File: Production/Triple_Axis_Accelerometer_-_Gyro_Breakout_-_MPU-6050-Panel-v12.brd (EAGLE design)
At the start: 116.8 x 107.7 mm, 459 parts, among them U1 MPU-6050-1, U10 MPU-6050-1, U11 MPU-6050-1, U12 MPU-6050-1, U13 MPU-6050-1, U14 MPU-6050-1, U15 MPU-6050-1, U16 MPU-6050-1, U17 MPU-6050-1, U18 MPU-6050-1, U19 MPU-6050-1, U2 MPU-6050-1, U20 MPU-6050-1, U21 MPU-6050-1, U22 MPU-6050-1, U23 MPU-6050-1, U24 MPU-6050-1, U3 MPU-6050-1, U4 MPU-6050-1, U5 MPU-6050-1, U6 MPU-6050-1, U7 MPU-6050-1, U8 MPU-6050-1, U9 MPU-6050-1

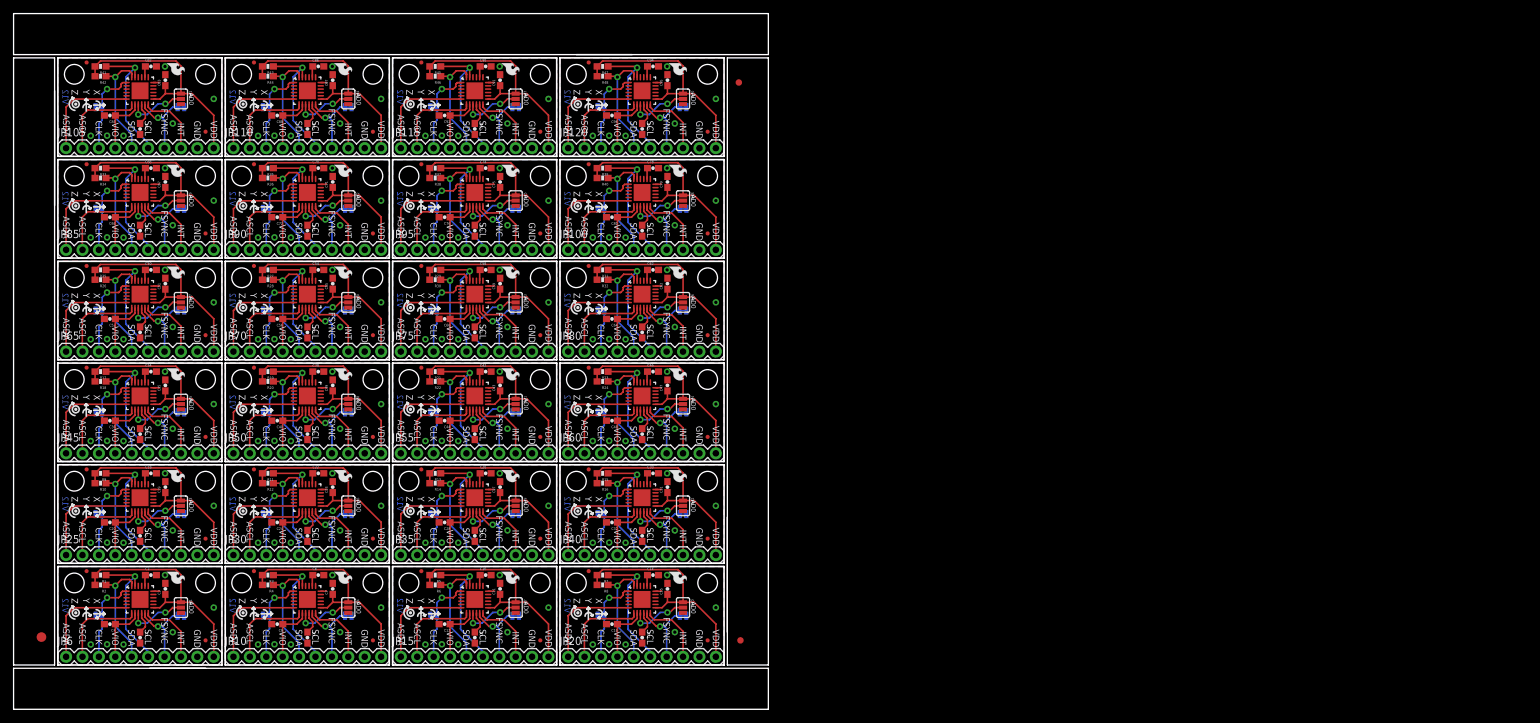
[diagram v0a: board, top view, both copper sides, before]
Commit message: changed panel for better solder printing
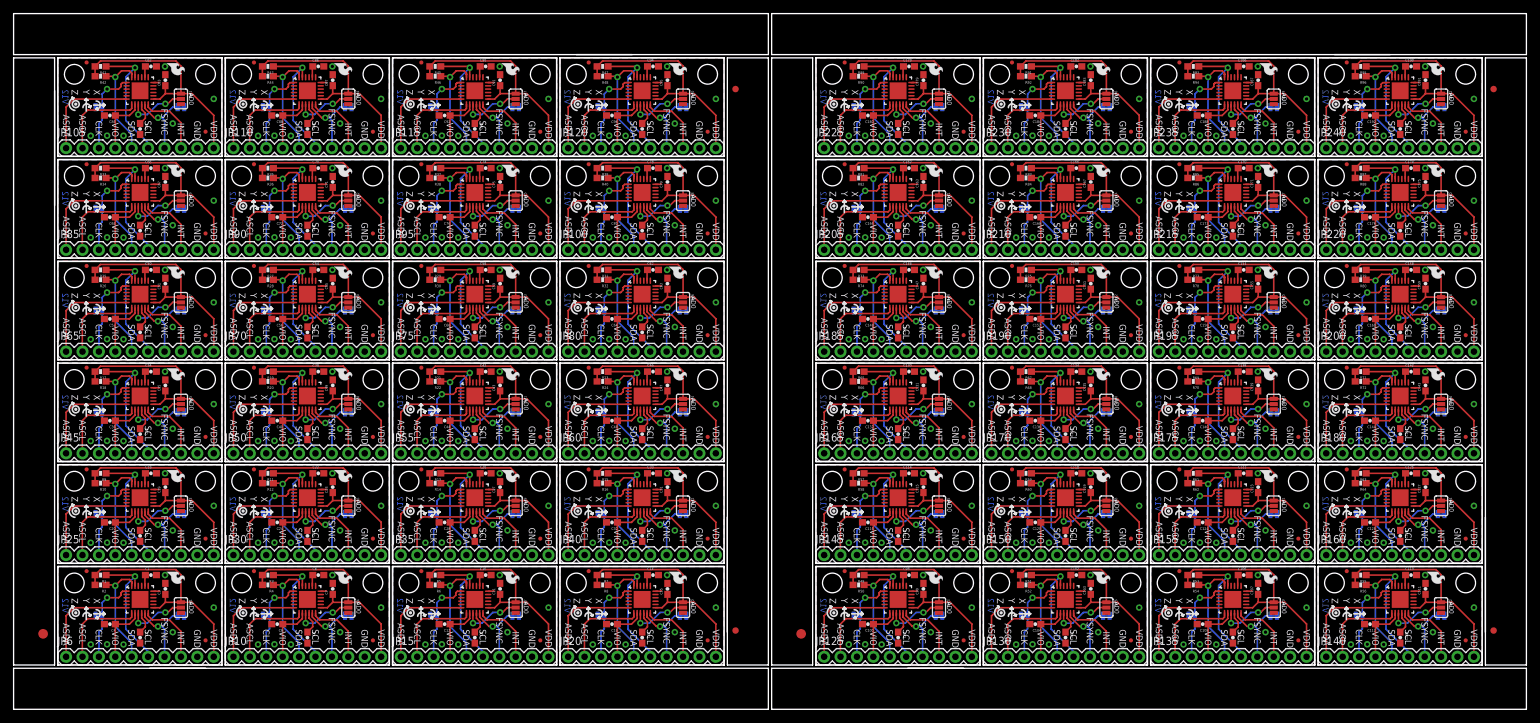
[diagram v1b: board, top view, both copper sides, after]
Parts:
- added C100, C104, C108, C112, C116, C120, C124, C128, C132, C136, C140, C144, C148, C152, C156, C160, C164, C168, C172, C176, C180, C184, C188, C192: 10nF, SparkFun:0603-CAP
- added C101, C103, C105, C107, C109, C111, C113, C115, C117, C119, C121, C123, C125, C127, C129, C131, C133, C135, C137, C139, C141, C143, C145, C147, C149, C151, C153, C155, C157, C159, C161, C163, C165, C167, C169, C171, C173, C175, C177, C179, C181, C183, C185, C187, C189, C191, C97, C99: 0.1uF, SparkFun:0603-CAP
- added C102, C106, C110, C114, C118, C122, C126, C130, C134, C138, C142, C146, C150, C154, C158, C162, C166, C170, C174, C178, C182, C186, C190, C98: 2.2nF, SparkFun:0603-CAP
- added E$2, E$3: (no value), SparkFun-Aesthetics:FIDUCIAL-1X2
- added E$6: (no value), SparkFun-Aesthetics:FIDUCIAL-1.5X3
- added JP121, JP122, JP126, JP127, JP131, JP132, JP136, JP137, JP141, JP142, JP146, JP147, JP151, JP152, JP156, JP157, JP161, JP162, JP166, JP167, JP171, JP172, JP176, JP177, JP181, JP182, JP186, JP187, JP191, JP192, JP196, JP197, JP201, JP202, JP206, JP207, JP211, JP212, JP216, JP217, JP221, JP222, JP226, JP227, JP231, JP232, JP236, JP237: STAND-OFFTIGHT, SparkFun:STAND-OFF-TIGHT
- added JP123, JP124, JP128, JP129, JP133, JP134, JP138, JP139, JP143, JP144, JP148, JP149, JP153, JP154, JP158, JP159, JP163, JP164, JP168, JP169, JP173, JP174, JP178, JP179, JP183, JP184, JP188, JP189, JP193, JP194, JP198, JP199, JP203, JP204, JP208, JP209, JP213, JP214, JP218, JP219, JP223, JP224, JP228, JP229, JP233, JP234, JP238, JP239: FIDUCIALUFIDUCIAL, SparkFun:MICRO-FIDUCIAL
- added JP125, JP130, JP135, JP140, JP145, JP150, JP155, JP160, JP165, JP170, JP175, JP180, JP185, JP190, JP195, JP200, JP205, JP210, JP215, JP220, JP225, JP230, JP235, JP240: M10", SparkFun:1X10
- added R49, R50, R51, R52, R53, R54, R55, R56, R57, R58, R59, R60, R61, R62, R63, R64, R65, R66, R67, R68, R69, R70, R71, R72, R73, R74, R75, R76, R77, R78, R79, R80, R81, R82, R83, R84, R85, R86, R87, R88, R89, R90, R91, R92, R93, R94, R95, R96: 10k, SparkFun:0603-RES
- added SJ100, SJ103, SJ106, SJ109, SJ112, SJ115, SJ118, SJ121, SJ124, SJ127, SJ130, SJ133, SJ136, SJ139, SJ142, SJ73, SJ76, SJ79, SJ82, SJ85, SJ88, SJ91, SJ94, SJ97: (no value), SparkFun:SJ_3_PASTE2&3
- added SJ101, SJ102, SJ104, SJ105, SJ107, SJ108, SJ110, SJ111, SJ113, SJ114, SJ116, SJ117, SJ119, SJ120, SJ122, SJ123, SJ125, SJ126, SJ128, SJ129, SJ131, SJ132, SJ134, SJ135, SJ137, SJ138, SJ140, SJ141, SJ143, SJ144, SJ74, SJ75, SJ77, SJ78, SJ80, SJ81, SJ83, SJ84, SJ86, SJ87, SJ89, SJ90, SJ92, SJ93, SJ95, SJ96, SJ98, SJ99: (no value), SparkFun:SJ_2S-TRACE
- added U$100, U$104, U$108, U$112, U$116, U$120, U$124, U$128, U$132, U$136, U$140, U$144, U$148, U$152, U$156, U$160, U$164, U$168, U$172, U$176, U$180, U$184, U$188, U$192: (no value), SparkFun:SFE-NEW-WEB
- added U$101, U$103, U$105, U$107, U$109, U$111, U$113, U$115, U$117, U$119, U$121, U$123, U$125, U$127, U$129, U$131, U$133, U$135, U$137, U$139, U$141, U$143, U$145, U$147, U$149, U$151, U$153, U$155, U$157, U$159, U$161, U$163, U$165, U$167, U$169, U$171, U$173, U$175, U$177, U$179, U$181, U$183, U$185, U$187, U$189, U$191, U$97, U$99: (no value), SparkFun:SFE-LOGO-FLAME
- added U$102, U$106, U$110, U$114, U$118, U$122, U$126, U$130, U$134, U$138, U$142, U$146, U$150, U$154, U$158, U$162, U$166, U$170, U$174, U$178, U$182, U$186, U$190, U$98: OSHW-LOGOS, SparkFun:OSHW-LOGO-S
- added U25, U26, U27, U28, U29, U30, U31, U32, U33, U34, U35, U36, U37, U38, U39, U40, U41, U42, U43, U44, U45, U46, U47, U48: MPU-6050-1, Testing:QFN-24-4MM2
- moved E$4 1.70 mm to (111.8, 12.2)
- moved E$5 1.14 mm to (111.8, 96.0)
- moved E$1 0.57 mm to (4.57, 11.7)
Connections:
- new net ADO24: SJ73.2, U25.9
- new net ADO25: SJ76.2, U26.9
- new net ADO26: SJ79.2, U27.9
- new net ADO27: SJ82.2, U28.9
- new net ADO28: SJ85.2, U29.9
- new net ADO29: SJ88.2, U30.9
- new net ADO30: SJ91.2, U31.9
- new net ADO31: SJ94.2, U32.9
- new net ADO32: SJ97.2, U33.9
- new net ADO33: SJ100.2, U34.9
- new net ADO34: SJ103.2, U35.9
- new net ADO35: SJ106.2, U36.9
- new net ADO36: SJ109.2, U37.9
- new net ADO37: SJ112.2, U38.9
- new net ADO38: SJ115.2, U39.9
- new net ADO39: SJ118.2, U40.9
- new net ADO40: SJ121.2, U41.9
- new net ADO41: SJ124.2, U42.9
- new net ADO42: SJ127.2, U43.9
- new net ADO43: SJ130.2, U44.9
- new net ADO44: SJ133.2, U45.9
- new net ADO45: SJ136.2, U46.9
- new net ADO46: SJ139.2, U47.9
- new net ADO47: SJ142.2, U48.9
- new net AUX_SCL24: JP125.2, U25.7
- new net AUX_SCL25: JP130.2, U26.7
- new net AUX_SCL26: JP135.2, U27.7
- new net AUX_SCL27: JP140.2, U28.7
- new net AUX_SCL28: JP145.2, U29.7
- new net AUX_SCL29: JP150.2, U30.7
- new net AUX_SCL30: JP155.2, U31.7
- new net AUX_SCL31: JP160.2, U32.7
- new net AUX_SCL32: JP165.2, U33.7
- new net AUX_SCL33: JP170.2, U34.7
- new net AUX_SCL34: JP175.2, U35.7
- new net AUX_SCL35: JP180.2, U36.7
- new net AUX_SCL36: JP185.2, U37.7
- new net AUX_SCL37: JP190.2, U38.7
- new net AUX_SCL38: JP195.2, U39.7
- new net AUX_SCL39: JP200.2, U40.7
- new net AUX_SCL40: JP205.2, U41.7
- new net AUX_SCL41: JP210.2, U42.7
- new net AUX_SCL42: JP215.2, U43.7
- new net AUX_SCL43: JP220.2, U44.7
- new net AUX_SCL44: JP225.2, U45.7
- new net AUX_SCL45: JP230.2, U46.7
- new net AUX_SCL46: JP235.2, U47.7
- new net AUX_SCL47: JP240.2, U48.7
- new net AUX_SDA24: JP125.1, U25.6
- new net AUX_SDA25: JP130.1, U26.6
- new net AUX_SDA26: JP135.1, U27.6
- new net AUX_SDA27: JP140.1, U28.6
- new net AUX_SDA28: JP145.1, U29.6
- new net AUX_SDA29: JP150.1, U30.6
- new net AUX_SDA30: JP155.1, U31.6
- new net AUX_SDA31: JP160.1, U32.6
- new net AUX_SDA32: JP165.1, U33.6
- new net AUX_SDA33: JP170.1, U34.6
- new net AUX_SDA34: JP175.1, U35.6
- new net AUX_SDA35: JP180.1, U36.6
- new net AUX_SDA36: JP185.1, U37.6
- new net AUX_SDA37: JP190.1, U38.6
- new net AUX_SDA38: JP195.1, U39.6
- new net AUX_SDA39: JP200.1, U40.6
- new net AUX_SDA40: JP205.1, U41.6
- new net AUX_SDA41: JP210.1, U42.6
- new net AUX_SDA42: JP215.1, U43.6
- new net AUX_SDA43: JP220.1, U44.6
- new net AUX_SDA44: JP225.1, U45.6
- new net AUX_SDA45: JP230.1, U46.6
- new net AUX_SDA46: JP235.1, U47.6
- new net AUX_SDA47: JP240.1, U48.6
- new net CLKIN24: JP125.3, SJ75.2, U25.1
- new net CLKIN25: JP130.3, SJ78.2, U26.1
- new net CLKIN26: JP135.3, SJ81.2, U27.1
- new net CLKIN27: JP140.3, SJ84.2, U28.1
- new net CLKIN28: JP145.3, SJ87.2, U29.1
- new net CLKIN29: JP150.3, SJ90.2, U30.1
- new net CLKIN30: JP155.3, SJ93.2, U31.1
- new net CLKIN31: JP160.3, SJ96.2, U32.1
- new net CLKIN32: JP165.3, SJ99.2, U33.1
- new net CLKIN33: JP170.3, SJ102.2, U34.1
- new net CLKIN34: JP175.3, SJ105.2, U35.1
- new net CLKIN35: JP180.3, SJ108.2, U36.1
- new net CLKIN36: JP185.3, SJ111.2, U37.1
- new net CLKIN37: JP190.3, SJ114.2, U38.1
- new net CLKIN38: JP195.3, SJ117.2, U39.1
- new net CLKIN39: JP200.3, SJ120.2, U40.1
- new net CLKIN40: JP205.3, SJ123.2, U41.1
- new net CLKIN41: JP210.3, SJ126.2, U42.1
- new net CLKIN42: JP215.3, SJ129.2, U43.1
- new net CLKIN43: JP220.3, SJ132.2, U44.1
- new net CLKIN44: JP225.3, SJ135.2, U45.1
- new net CLKIN45: JP230.3, SJ138.2, U46.1
- new net CLKIN46: JP235.3, SJ141.2, U47.1
- new net CLKIN47: JP240.3, SJ144.2, U48.1
- new net FSYNC24: JP125.7, SJ74.2, U25.11
- new net FSYNC25: JP130.7, SJ77.2, U26.11
- new net FSYNC26: JP135.7, SJ80.2, U27.11
- new net FSYNC27: JP140.7, SJ83.2, U28.11
- new net FSYNC28: JP145.7, SJ86.2, U29.11
- new net FSYNC29: JP150.7, SJ89.2, U30.11
- new net FSYNC30: JP155.7, SJ92.2, U31.11
- new net FSYNC31: JP160.7, SJ95.2, U32.11
- new net FSYNC32: JP165.7, SJ98.2, U33.11
- new net FSYNC33: JP170.7, SJ101.2, U34.11
- new net FSYNC34: JP175.7, SJ104.2, U35.11
- new net FSYNC35: JP180.7, SJ107.2, U36.11
- new net FSYNC36: JP185.7, SJ110.2, U37.11
- new net FSYNC37: JP190.7, SJ113.2, U38.11
- new net FSYNC38: JP195.7, SJ116.2, U39.11
- new net FSYNC39: JP200.7, SJ119.2, U40.11
- new net FSYNC40: JP205.7, SJ122.2, U41.11
- new net FSYNC41: JP210.7, SJ125.2, U42.11
- new net FSYNC42: JP215.7, SJ128.2, U43.11
- new net FSYNC43: JP220.7, SJ131.2, U44.11
- new net FSYNC44: JP225.7, SJ134.2, U45.11
- new net FSYNC45: JP230.7, SJ137.2, U46.11
- new net FSYNC46: JP235.7, SJ140.2, U47.11
- new net FSYNC47: JP240.7, SJ143.2, U48.11
- new net GND24: C100.2, C97.2, C98.2, C99.2, JP125.9, SJ73.3, SJ74.1, SJ75.1, U25.18
- new net GND25: C101.2, C102.2, C103.2, C104.2, JP130.9, SJ76.3, SJ77.1, SJ78.1, U26.18
- new net GND26: C105.2, C106.2, C107.2, C108.2, JP135.9, SJ79.3, SJ80.1, SJ81.1, U27.18
- new net GND27: C109.2, C110.2, C111.2, C112.2, JP140.9, SJ82.3, SJ83.1, SJ84.1, U28.18
- new net GND28: C113.2, C114.2, C115.2, C116.2, JP145.9, SJ85.3, SJ86.1, SJ87.1, U29.18
- new net GND29: C117.2, C118.2, C119.2, C120.2, JP150.9, SJ88.3, SJ89.1, SJ90.1, U30.18
- new net GND30: C121.2, C122.2, C123.2, C124.2, JP155.9, SJ91.3, SJ92.1, SJ93.1, U31.18
- new net GND31: C125.2, C126.2, C127.2, C128.2, JP160.9, SJ94.3, SJ95.1, SJ96.1, U32.18
- new net GND32: C129.2, C130.2, C131.2, C132.2, JP165.9, SJ97.3, SJ98.1, SJ99.1, U33.18
- new net GND33: C133.2, C134.2, C135.2, C136.2, JP170.9, SJ100.3, SJ101.1, SJ102.1, U34.18
- new net GND34: C137.2, C138.2, C139.2, C140.2, JP175.9, SJ103.3, SJ104.1, SJ105.1, U35.18
- new net GND35: C141.2, C142.2, C143.2, C144.2, JP180.9, SJ106.3, SJ107.1, SJ108.1, U36.18
- new net GND36: C145.2, C146.2, C147.2, C148.2, JP185.9, SJ109.3, SJ110.1, SJ111.1, U37.18
- new net GND37: C149.2, C150.2, C151.2, C152.2, JP190.9, SJ112.3, SJ113.1, SJ114.1, U38.18
- new net GND38: C153.2, C154.2, C155.2, C156.2, JP195.9, SJ115.3, SJ116.1, SJ117.1, U39.18
- new net GND39: C157.2, C158.2, C159.2, C160.2, JP200.9, SJ118.3, SJ119.1, SJ120.1, U40.18
- new net GND40: C161.2, C162.2, C163.2, C164.2, JP205.9, SJ121.3, SJ122.1, SJ123.1, U41.18
- new net GND41: C165.2, C166.2, C167.2, C168.2, JP210.9, SJ124.3, SJ125.1, SJ126.1, U42.18
- new net GND42: C169.2, C170.2, C171.2, C172.2, JP215.9, SJ127.3, SJ128.1, SJ129.1, U43.18
- new net GND43: C173.2, C174.2, C175.2, C176.2, JP220.9, SJ130.3, SJ131.1, SJ132.1, U44.18
- new net GND44: C177.2, C178.2, C179.2, C180.2, JP225.9, SJ133.3, SJ134.1, SJ135.1, U45.18
- new net GND45: C181.2, C182.2, C183.2, C184.2, JP230.9, SJ136.3, SJ137.1, SJ138.1, U46.18
- new net GND46: C185.2, C186.2, C187.2, C188.2, JP235.9, SJ139.3, SJ140.1, SJ141.1, U47.18
- new net GND47: C189.2, C190.2, C191.2, C192.2, JP240.9, SJ142.3, SJ143.1, SJ144.1, U48.18
- new net INT24: JP125.8, U25.12
- new net INT25: JP130.8, U26.12
- new net INT26: JP135.8, U27.12
- new net INT27: JP140.8, U28.12
- new net INT28: JP145.8, U29.12
- new net INT29: JP150.8, U30.12
- new net INT30: JP155.8, U31.12
- new net INT31: JP160.8, U32.12
- new net INT32: JP165.8, U33.12
- new net INT33: JP170.8, U34.12
- new net INT34: JP175.8, U35.12
- new net INT35: JP180.8, U36.12
- new net INT36: JP185.8, U37.12
- new net INT37: JP190.8, U38.12
- new net INT38: JP195.8, U39.12
- new net INT39: JP200.8, U40.12
- new net INT40: JP205.8, U41.12
- new net INT41: JP210.8, U42.12
- new net INT42: JP215.8, U43.12
- new net INT43: JP220.8, U44.12
- new net INT44: JP225.8, U45.12
- new net INT45: JP230.8, U46.12
- new net INT46: JP235.8, U47.12
- new net INT47: JP240.8, U48.12
- new net N$49: C98.1, U25.20
- new net N$50: C97.1, U25.10
- new net N$51: C102.1, U26.20
- new net N$52: C101.1, U26.10
- new net N$53: C106.1, U27.20
- new net N$54: C105.1, U27.10
- new net N$55: C110.1, U28.20
- new net N$56: C109.1, U28.10
- new net N$57: C114.1, U29.20
- new net N$58: C113.1, U29.10
- new net N$59: C118.1, U30.20
- new net N$60: C117.1, U30.10
- new net N$61: C122.1, U31.20
- new net N$62: C121.1, U31.10
- new net N$63: C126.1, U32.20
- new net N$64: C125.1, U32.10
- new net N$65: C130.1, U33.20
- new net N$66: C129.1, U33.10
- new net N$67: C134.1, U34.20
- new net N$68: C133.1, U34.10
- new net N$69: C138.1, U35.20
- new net N$70: C137.1, U35.10
- new net N$71: C142.1, U36.20
- new net N$72: C141.1, U36.10
- new net N$73: C146.1, U37.20
- new net N$74: C145.1, U37.10
- new net N$75: C150.1, U38.20
- new net N$76: C149.1, U38.10
- new net N$77: C154.1, U39.20
- new net N$78: C153.1, U39.10
- new net N$79: C158.1, U40.20
- new net N$80: C157.1, U40.10
- new net N$81: C162.1, U41.20
- new net N$82: C161.1, U41.10
- new net N$83: C166.1, U42.20
- new net N$84: C165.1, U42.10
- new net N$85: C170.1, U43.20
- new net N$86: C169.1, U43.10
- new net N$87: C174.1, U44.20
- new net N$88: C173.1, U44.10
- new net N$89: C178.1, U45.20
- new net N$90: C177.1, U45.10
- new net N$91: C182.1, U46.20
- new net N$92: C181.1, U46.10
- new net N$93: C186.1, U47.20
- new net N$94: C185.1, U47.10
- new net N$95: C190.1, U48.20
- new net N$96: C189.1, U48.10
- new net SCL24: JP125.6, R49.1, U25.23
- new net SCL25: JP130.6, R51.1, U26.23
- new net SCL26: JP135.6, R53.1, U27.23
- new net SCL27: JP140.6, R55.1, U28.23
- new net SCL28: JP145.6, R57.1, U29.23
- new net SCL29: JP150.6, R59.1, U30.23
- new net SCL30: JP155.6, R61.1, U31.23
- new net SCL31: JP160.6, R63.1, U32.23
- new net SCL32: JP165.6, R65.1, U33.23
- new net SCL33: JP170.6, R67.1, U34.23
- new net SCL34: JP175.6, R69.1, U35.23
- new net SCL35: JP180.6, R71.1, U36.23
- new net SCL36: JP185.6, R73.1, U37.23
- new net SCL37: JP190.6, R75.1, U38.23
- new net SCL38: JP195.6, R77.1, U39.23
- new net SCL39: JP200.6, R79.1, U40.23
- new net SCL40: JP205.6, R81.1, U41.23
- new net SCL41: JP210.6, R83.1, U42.23
- new net SCL42: JP215.6, R85.1, U43.23
- new net SCL43: JP220.6, R87.1, U44.23
- new net SCL44: JP225.6, R89.1, U45.23
- new net SCL45: JP230.6, R91.1, U46.23
- new net SCL46: JP235.6, R93.1, U47.23
- new net SCL47: JP240.6, R95.1, U48.23
- new net SDA24: JP125.5, R50.1, U25.24
- new net SDA25: JP130.5, R52.1, U26.24
- new net SDA26: JP135.5, R54.1, U27.24
- new net SDA27: JP140.5, R56.1, U28.24
- new net SDA28: JP145.5, R58.1, U29.24
- new net SDA29: JP150.5, R60.1, U30.24
- new net SDA30: JP155.5, R62.1, U31.24
- new net SDA31: JP160.5, R64.1, U32.24
- new net SDA32: JP165.5, R66.1, U33.24
- new net SDA33: JP170.5, R68.1, U34.24
- new net SDA34: JP175.5, R70.1, U35.24
- new net SDA35: JP180.5, R72.1, U36.24
- new net SDA36: JP185.5, R74.1, U37.24
- new net SDA37: JP190.5, R76.1, U38.24
- new net SDA38: JP195.5, R78.1, U39.24
- new net SDA39: JP200.5, R80.1, U40.24
- new net SDA40: JP205.5, R82.1, U41.24
- new net SDA41: JP210.5, R84.1, U42.24
- new net SDA42: JP215.5, R86.1, U43.24
- new net SDA43: JP220.5, R88.1, U44.24
- new net SDA44: JP225.5, R90.1, U45.24
- new net SDA45: JP230.5, R92.1, U46.24
- new net SDA46: JP235.5, R94.1, U47.24
- new net SDA47: JP240.5, R96.1, U48.24
- new net VCC24: C99.1, JP125.10, R49.2, R50.2, SJ73.1, U25.13
- new net VCC25: C103.1, JP130.10, R51.2, R52.2, SJ76.1, U26.13
- new net VCC26: C107.1, JP135.10, R53.2, R54.2, SJ79.1, U27.13
- new net VCC27: C111.1, JP140.10, R55.2, R56.2, SJ82.1, U28.13
- new net VCC28: C115.1, JP145.10, R57.2, R58.2, SJ85.1, U29.13
- new net VCC29: C119.1, JP150.10, R59.2, R60.2, SJ88.1, U30.13
- new net VCC30: C123.1, JP155.10, R61.2, R62.2, SJ91.1, U31.13
- new net VCC31: C127.1, JP160.10, R63.2, R64.2, SJ94.1, U32.13
- new net VCC32: C131.1, JP165.10, R65.2, R66.2, SJ97.1, U33.13
- new net VCC33: C135.1, JP170.10, R67.2, R68.2, SJ100.1, U34.13
- new net VCC34: C139.1, JP175.10, R69.2, R70.2, SJ103.1, U35.13
- new net VCC35: C143.1, JP180.10, R71.2, R72.2, SJ106.1, U36.13
- new net VCC36: C147.1, JP185.10, R73.2, R74.2, SJ109.1, U37.13
- new net VCC37: C151.1, JP190.10, R75.2, R76.2, SJ112.1, U38.13
- new net VCC38: C155.1, JP195.10, R77.2, R78.2, SJ115.1, U39.13
- new net VCC39: C159.1, JP200.10, R79.2, R80.2, SJ118.1, U40.13
- new net VCC40: C163.1, JP205.10, R81.2, R82.2, SJ121.1, U41.13
- new net VCC41: C167.1, JP210.10, R83.2, R84.2, SJ124.1, U42.13
- new net VCC42: C171.1, JP215.10, R85.2, R86.2, SJ127.1, U43.13
- new net VCC43: C175.1, JP220.10, R87.2, R88.2, SJ130.1, U44.13
- new net VCC44: C179.1, JP225.10, R89.2, R90.2, SJ133.1, U45.13
- new net VCC45: C183.1, JP230.10, R91.2, R92.2, SJ136.1, U46.13
- new net VCC46: C187.1, JP235.10, R93.2, R94.2, SJ139.1, U47.13
- new net VCC47: C191.1, JP240.10, R95.2, R96.2, SJ142.1, U48.13
- new net VIO24: C100.1, JP125.4, U25.8
- new net VIO25: C104.1, JP130.4, U26.8
- new net VIO26: C108.1, JP135.4, U27.8
- new net VIO27: C112.1, JP140.4, U28.8
- new net VIO28: C116.1, JP145.4, U29.8
- new net VIO29: C120.1, JP150.4, U30.8
- new net VIO30: C124.1, JP155.4, U31.8
- new net VIO31: C128.1, JP160.4, U32.8
- new net VIO32: C132.1, JP165.4, U33.8
- new net VIO33: C136.1, JP170.4, U34.8
- new net VIO34: C140.1, JP175.4, U35.8
- new net VIO35: C144.1, JP180.4, U36.8
- new net VIO36: C148.1, JP185.4, U37.8
- new net VIO37: C152.1, JP190.4, U38.8
- new net VIO38: C156.1, JP195.4, U39.8
- new net VIO39: C160.1, JP200.4, U40.8
- new net VIO40: C164.1, JP205.4, U41.8
- new net VIO41: C168.1, JP210.4, U42.8
- new net VIO42: C172.1, JP215.4, U43.8
- new net VIO43: C176.1, JP220.4, U44.8
- new net VIO44: C180.1, JP225.4, U45.8
- new net VIO45: C184.1, JP230.4, U46.8
- new net VIO46: C188.1, JP235.4, U47.8
- new net VIO47: C192.1, JP240.4, U48.8
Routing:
- net VCC47: track 0.00 -> 37.5 mm
- net VCC44: track 0.00 -> 37.5 mm
- net VCC45: track 0.00 -> 37.5 mm
- net VCC35: track 0.00 -> 37.5 mm
- net VCC31: track 0.00 -> 37.5 mm
- net VCC27: track 0.00 -> 37.5 mm
- net VCC46: track 0.00 -> 37.5 mm
- net VCC28: track 0.00 -> 37.5 mm
- net VCC43: track 0.00 -> 37.5 mm
- net VCC32: track 0.00 -> 37.5 mm
- net VCC24: track 0.00 -> 37.5 mm
- net VCC39: track 0.00 -> 37.5 mm
- net VCC40: track 0.00 -> 37.5 mm
- net VCC36: track 0.00 -> 37.5 mm
- net VCC34: track 0.00 -> 37.5 mm
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- added copper zone on layer 1, net GND24
- added copper zone on layer 16, net GND24
- added copper zone on layer 1, net GND25
- added copper zone on layer 16, net GND25
- added copper zone on layer 1, net GND26
- added copper zone on layer 16, net GND26
- added copper zone on layer 1, net GND27
- added copper zone on layer 16, net GND27
- added copper zone on layer 1, net GND28
- added copper zone on layer 16, net GND28
- added copper zone on layer 1, net GND29
- added copper zone on layer 16, net GND29
- added copper zone on layer 1, net GND30
- added copper zone on layer 16, net GND30
- added copper zone on layer 1, net GND31
- added copper zone on layer 16, net GND31
- added copper zone on layer 1, net GND32
- added copper zone on layer 16, net GND32
- added copper zone on layer 1, net GND33
- added copper zone on layer 16, net GND33
- added copper zone on layer 1, net GND34
- added copper zone on layer 16, net GND34
- added copper zone on layer 1, net GND35
- added copper zone on layer 16, net GND35
- added copper zone on layer 1, net GND36
- added copper zone on layer 16, net GND36
- added copper zone on layer 1, net GND37
- added copper zone on layer 16, net GND37
- added copper zone on layer 1, net GND38
- added copper zone on layer 16, net GND38
- added copper zone on layer 1, net GND39
- added copper zone on layer 16, net GND39
- added copper zone on layer 1, net GND40
- added copper zone on layer 16, net GND40
- added copper zone on layer 1, net GND41
- added copper zone on layer 16, net GND41
- added copper zone on layer 1, net GND42
- added copper zone on layer 16, net GND42
- added copper zone on layer 1, net GND43
- added copper zone on layer 16, net GND43
- added copper zone on layer 1, net GND44
- added copper zone on layer 16, net GND44
- added copper zone on layer 1, net GND45
- added copper zone on layer 16, net GND45
- added copper zone on layer 1, net GND46
- added copper zone on layer 16, net GND46
- added copper zone on layer 1, net GND47
- added copper zone on layer 16, net GND47
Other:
- board size 116.8 x 107.7 mm -> 234.2 x 107.7 mm
